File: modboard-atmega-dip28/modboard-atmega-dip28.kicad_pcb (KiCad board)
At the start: 2 copper layers, 57.5 x 51.6 mm, 11 parts, among them J1 modboard-edge-connector, J2 Conn_01x03_Male, U1 ATMEGA328P-PU, Y1 Crystal

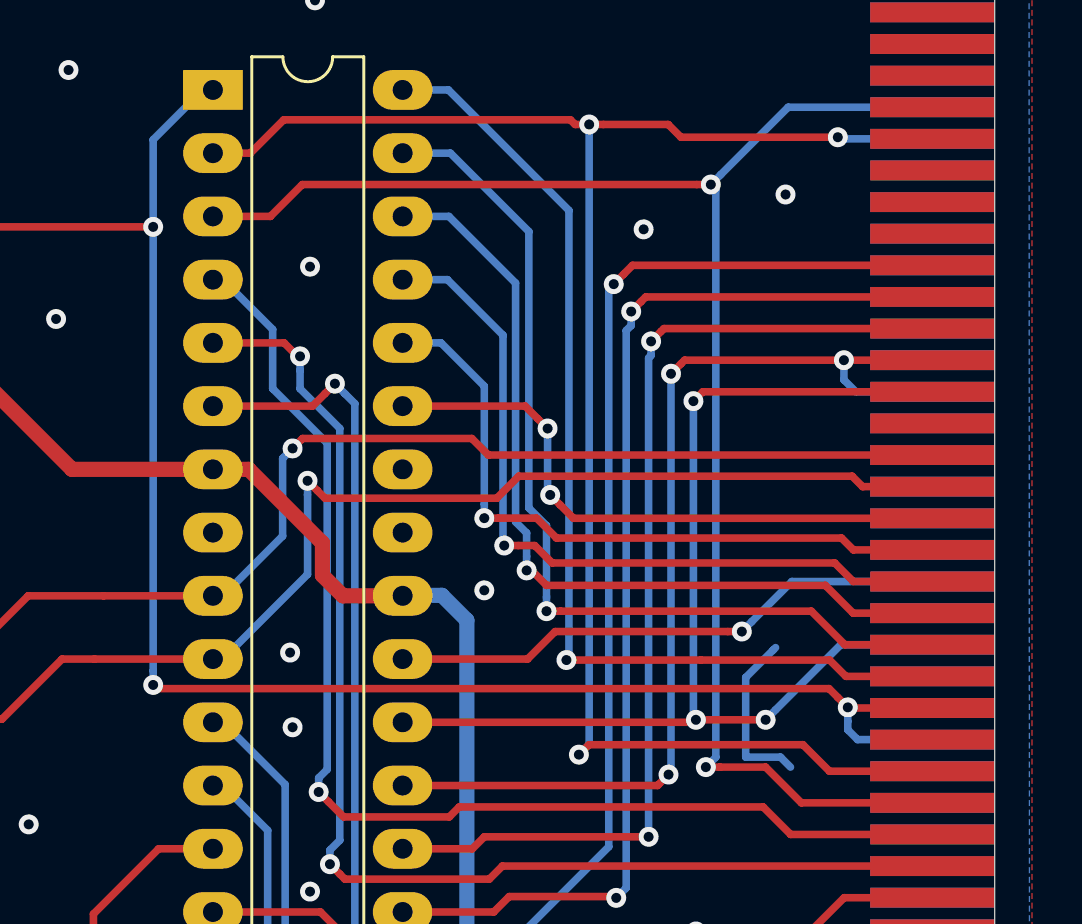
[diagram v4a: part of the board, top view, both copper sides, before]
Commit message: Routed edge connectors 44 (RESET) and 37 (PORTB_6)
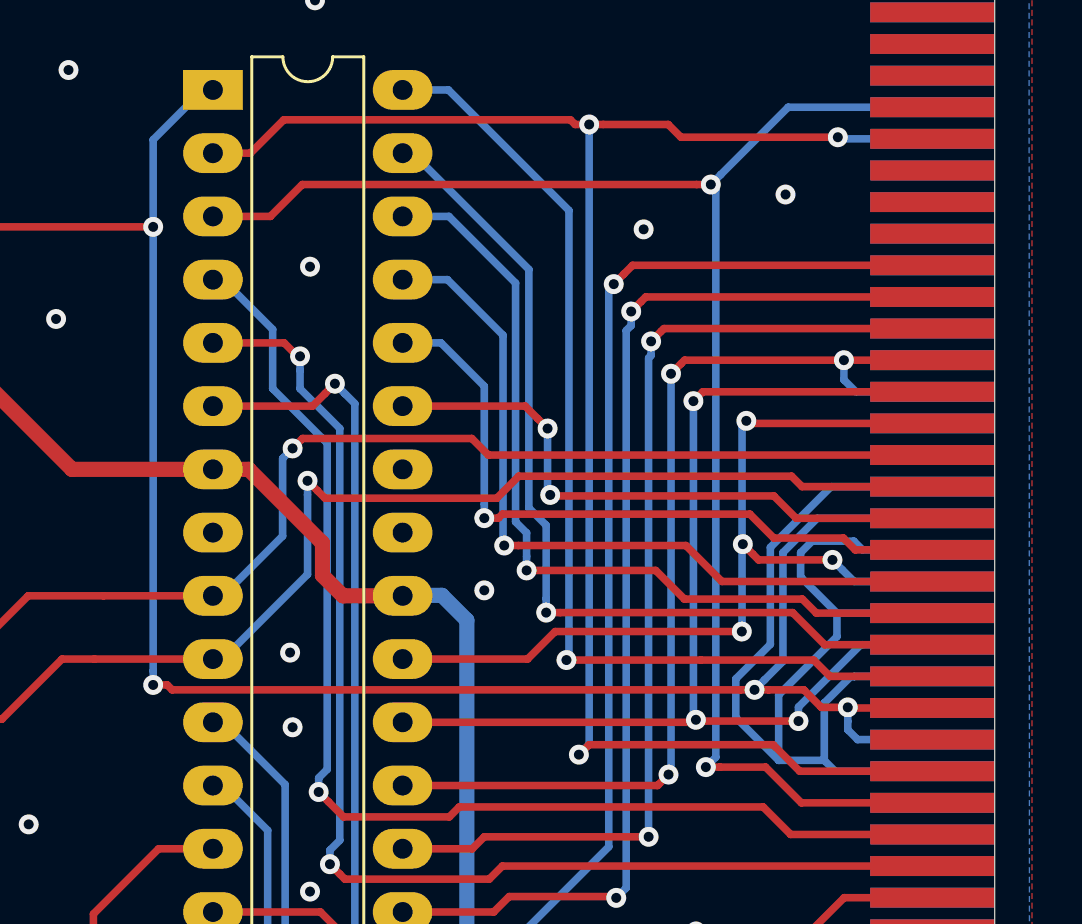
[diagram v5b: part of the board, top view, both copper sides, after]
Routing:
- net GND: track 6.86 -> 50.2 mm
- net SCK: track 22.6 -> 38.4 mm, vias 1 -> 4
- net RESET: track 68.5 -> 81.0 mm, vias 3 -> 4
- net Net-(J1-Pad51): track 38.0 -> 37.1 mm
